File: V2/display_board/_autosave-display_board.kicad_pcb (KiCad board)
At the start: 2 copper layers, 95 x 103.5 mm, 55 parts, among them J1 Conn_01x12, J2 Conn_01x12, Q1 Si1308EDL, SW1 SW_Push, SW2 SW_Push, SW3 SW_Push, SW4 SW_Push, U1 TPS61165DBV, U2 LTR-303ALS-01, U3 DS18B20Z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

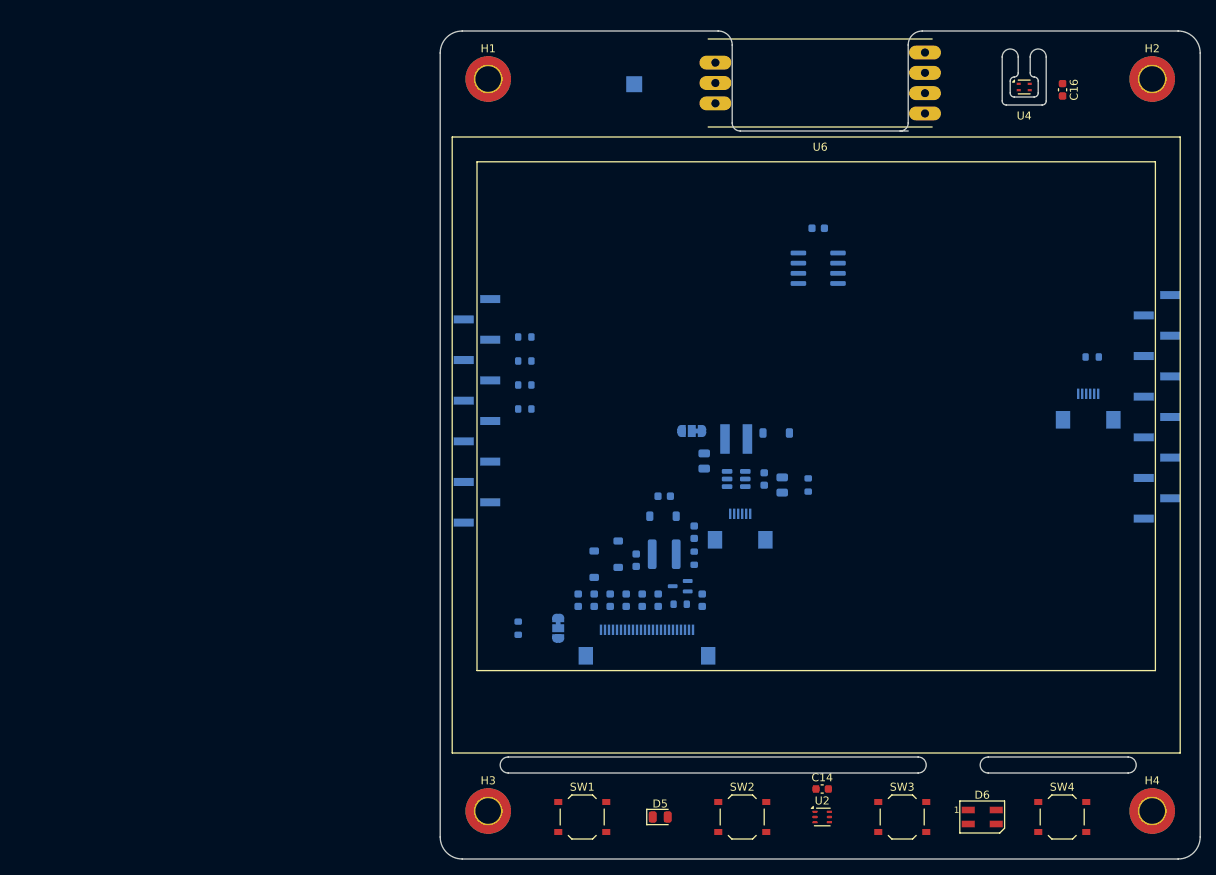
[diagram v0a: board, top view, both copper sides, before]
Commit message: Initial component placement done.
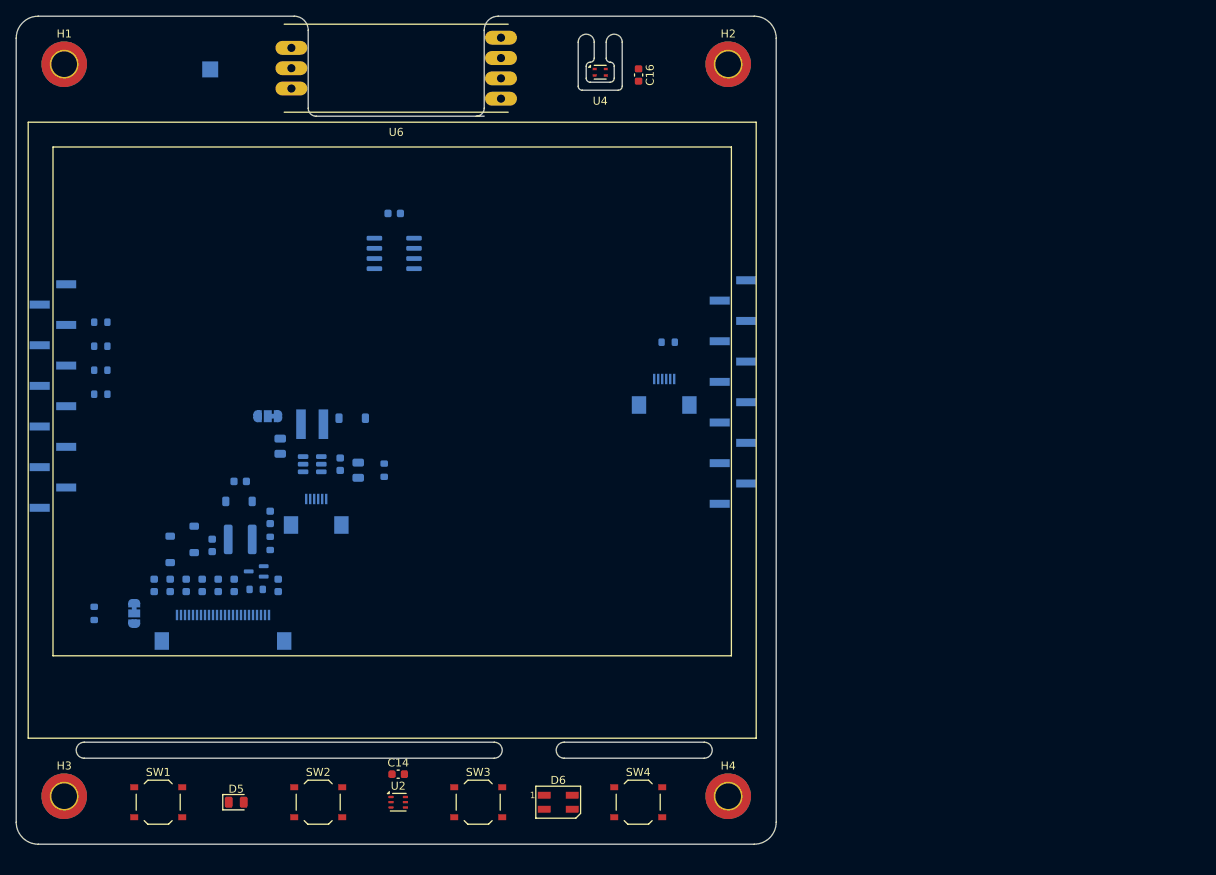
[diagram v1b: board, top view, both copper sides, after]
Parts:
- moved C16 53.0 mm to (127.8, 57.4)
- moved C1 53.0 mm to (81.8, 112.7)
- moved C10 53.0 mm to (82.8, 121.2)
- moved C11 53.0 mm to (83.0, 103.8)
- moved C12 53.0 mm to (90.5, 106.0)
- moved C13 53.0 mm to (92.8, 106.8)
- moved C14 53.0 mm to (97.8, 144.8)
- moved C15 53.0 mm to (97.2, 74.7)
- moved C2 53.0 mm to (74.5, 116.2)
- moved C3 53.0 mm to (78.0, 108.2)
- moved C4 53.0 mm to (77.2, 121.2)
- moved C5 53.0 mm to (75.2, 121.2)
- moved C6 53.0 mm to (73.2, 121.2)
- moved C7 53.0 mm to (69.2, 121.2)
- moved C8 53.0 mm to (71.2, 121.2)
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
